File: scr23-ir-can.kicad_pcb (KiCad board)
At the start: 2 copper layers, 27.4 x 27.4 mm, 22 parts, among them J1 22-24AWG, J2 22-24AWG, J3 22-24AWG, J4 22-24AWG, J6 Conn_ST_STDC14, U1 Sparkfun MLX90640 Breakout, U2 AP63205WU, U4 ADM3051CRZ, U5 STM32L431KBUx, U6 AP2127K-3.3

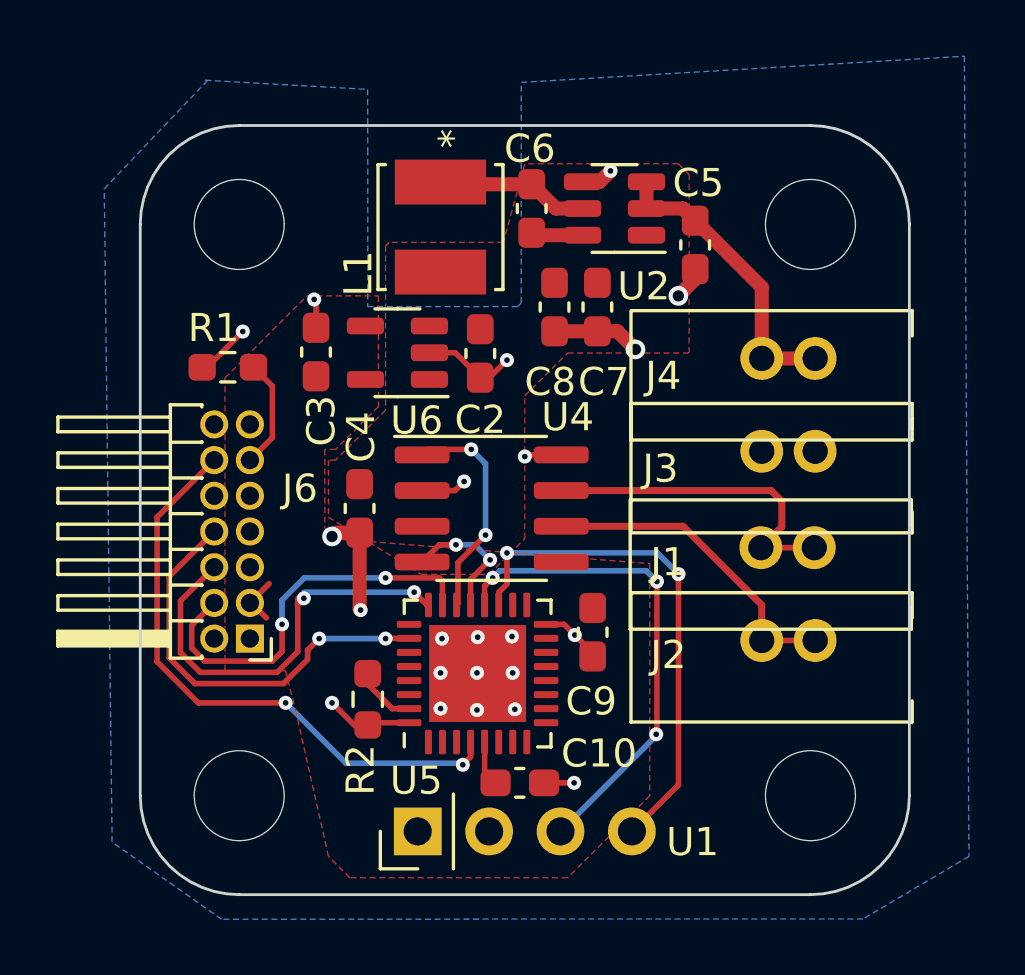
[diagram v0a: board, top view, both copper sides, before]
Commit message: add labels to the solderright bois
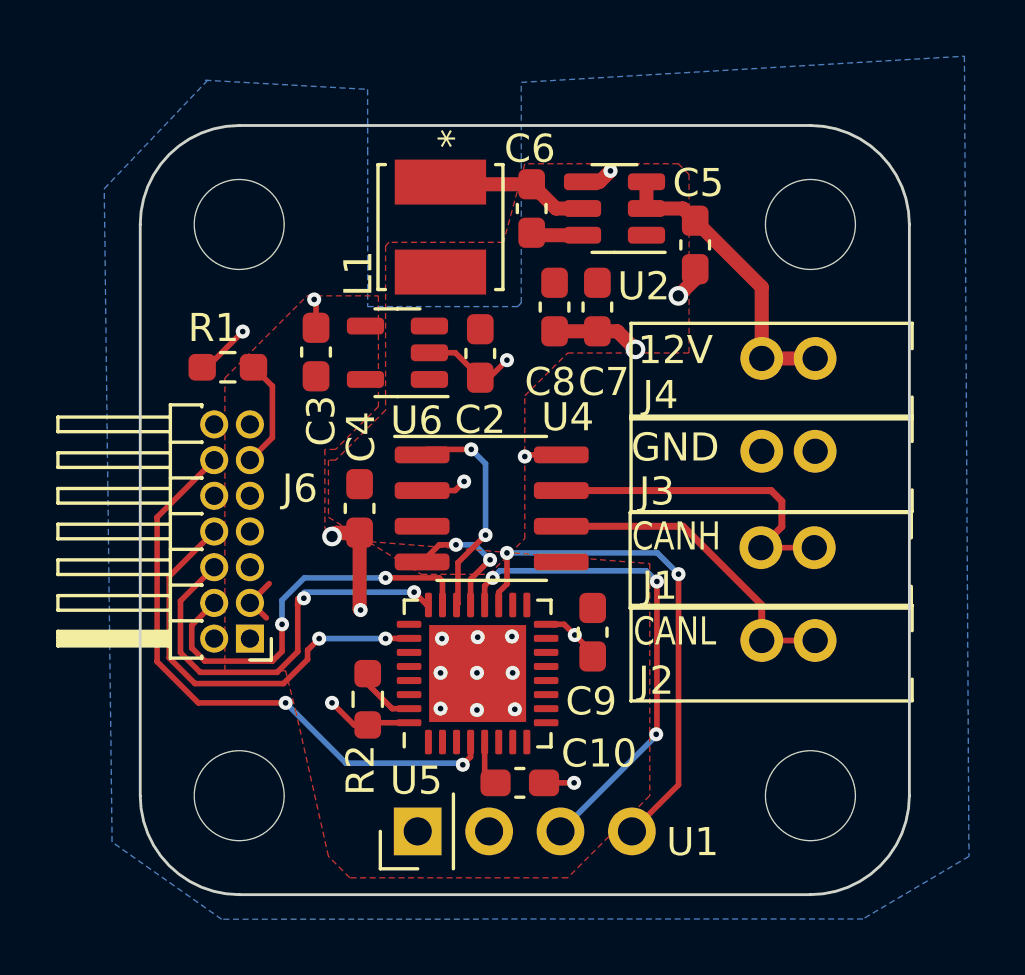
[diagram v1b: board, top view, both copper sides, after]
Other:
- board text added: "12V"
- board text added: "CANH"
- board text added: "CANL"
- board text added: "GND"
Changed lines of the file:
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@@
     (property "ki_description" "CONN TERM WTB 22-24AWG TIN")
     (attr through_hole)
-    (fp_text reference "J1" (at -3.2918 0.5167 unlocked) (layer "F.SilkS")
+    (fp_text reference "J1" (at -3.5966 1.3549 unlocked) (layer "F.SilkS")
         (effects (font (size 1 1) (thickness 0.15)))
     )
@@
         (effects (font (size 1 1) (thickness 0.15)))
     )
-    (fp_line (start -4.65 -1.7) (end 5.35 -1.7)
-      (stroke (width 0.12) (type default)) (layer "F.SilkS"))
-    (fp_line (start -4.65 2.9) (end -4.65 -1.65)
-      (stroke (width 0.12) (type default)) (layer "F.SilkS"))
-    (fp_line (start 5.35 -1.7) (end 5.35 -0.8)
-      (stroke (width 0.12) (type default)) (layer "F.SilkS"))
-    (fp_line (start 5.35 2.15) (end 5.35 2.9)
-      (stroke (width 0.12) (type default)) (layer "F.SilkS"))
-    (fp_line (start 5.35 2.9) (end -4.65 2.9)
+    (fp_line (start -4.65 -1.25) (end 5.35 -1.25)
+      (stroke (width 0.12) (type default)) (layer "F.SilkS"))
+    (fp_line (start -4.65 2.15) (end -4.65 -1.25)
+      (stroke (width 0.12) (type default)) (layer "F.SilkS"))
+    (fp_line (start 5.35 -1.25) (end 5.35 -0.35)
+      (stroke (width 0.12) (type default)) (layer "F.SilkS"))
+    (fp_line (start 5.35 1.375) (end 5.35 2.125)
+      (stroke (width 0.12) (type default)) (layer "F.SilkS"))
+    (fp_line (start 5.35 2.15) (end -4.65 2.15)
       (stroke (width 0.12) (type default)) (layer "F.SilkS"))
     (pad "1" thru_hole circle (at 0 0) (size 1.524 1.524) (drill 0.9) (layers "*.Cu" "*.Mask")
@@
     (property "ki_description" "CONN TERM WTB 22-24AWG TIN")
     (attr through_hole)
-    (fp_text reference "J4" (at -3.5006 0.6183 unlocked) (layer "F.SilkS")
+    (fp_text reference "J4" (at -3.6022 1.3041 unlocked) (layer "F.SilkS")
         (effects (font (size 1 1) (thickness 0.15)))
     )
@@
         (effects (font (size 1 1) (thickness 0.15)))
     )
-    (fp_line (start -4.65 -1.7) (end 5.35 -1.7)
-      (stroke (width 0.12) (type default)) (layer "F.SilkS"))
-    (fp_line (start -4.65 2.9) (end -4.65 -1.65)
-      (stroke (width 0.12) (type default)) (layer "F.SilkS"))
-    (fp_line (start 5.35 -1.7) (end 5.35 -0.8)
-      (stroke (width 0.12) (type default)) (layer "F.SilkS"))
-    (fp_line (start 5.35 2.15) (end 5.35 2.9)
-      (stroke (width 0.12) (type default)) (layer "F.SilkS"))
-    (fp_line (start 5.35 2.9) (end -4.65 2.9)
+    (fp_line (start -4.65 -1.25) (end 5.35 -1.25)
+      (stroke (width 0.12) (type default)) (layer "F.SilkS"))
+    (fp_line (start -4.65 2.15) (end -4.65 -1.25)
+      (stroke (width 0.12) (type default)) (layer "F.SilkS"))
+    (fp_line (start 5.35 -1.25) (end 5.35 -0.35)
+      (stroke (width 0.12) (type default)) (layer "F.SilkS"))
+    (fp_line (start 5.35 1.375) (end 5.35 2.125)
+      (stroke (width 0.12) (type default)) (layer "F.SilkS"))
+    (fp_line (start 5.35 2.15) (end -4.65 2.15)
       (stroke (width 0.12) (type default)) (layer "F.SilkS"))
     (pad "1" thru_hole circle (at 0 0) (size 1.524 1.524) (drill 0.9) (layers "*.Cu" "*.Mask")
@@
     (property "ki_description" "CONN TERM WTB 22-24AWG TIN")
     (attr through_hole)
-    (fp_text reference "J2" (at -3.3228 0.5167 unlocked) (layer "F.SilkS")
+    (fp_text reference "J2" (at -3.7546 1.4311 unlocked) (layer "F.SilkS")
         (effects (font (size 1 1) (thickness 0.15)))
     )
@@
         (effects (font (size 1 1) (thickness 0.15)))
     )
-    (fp_line (start -4.65 -1.7) (end 5.35 -1.7)
-      (stroke (width 0.12) (type default)) (layer "F.SilkS"))
-    (fp_line (start -4.65 2.9) (end -4.65 -1.65)
-      (stroke (width 0.12) (type default)) (layer "F.SilkS"))
-    (fp_line (start 5.35 -1.7) (end 5.35 -0.8)
-      (stroke (width 0.12) (type default)) (layer "F.SilkS"))
-    (fp_line (start 5.35 2.15) (end 5.35 2.9)
-      (stroke (width 0.12) (type default)) (layer "F.SilkS"))
-    (fp_line (start 5.35 2.9) (end -4.65 2.9)
+    (fp_line (start -4.65 -1.25) (end 5.35 -1.25)
+      (stroke (width 0.12) (type default)) (layer "F.SilkS"))
+    (fp_line (start -4.65 2.15) (end -4.65 -1.25)
+      (stroke (width 0.12) (type default)) (layer "F.SilkS"))
+    (fp_line (start 5.35 -1.25) (end 5.35 -0.35)
+      (stroke (width 0.12) (type default)) (layer "F.SilkS"))
+    (fp_line (start 5.35 1.375) (end 5.35 2.125)
+      (stroke (width 0.12) (type default)) (layer "F.SilkS"))
+    (fp_line (start 5.35 2.15) (end -4.65 2.15)
       (stroke (width 0.12) (type default)) (layer "F.SilkS"))
     (pad "1" thru_hole circle (at 0 0) (size 1.524 1.524) (drill 0.9) (layers "*.Cu" "*.Mask")
@@
     (property "ki_description" "CONN TERM WTB 22-24AWG TIN")
     (attr through_hole)
-    (fp_text reference "J3" (at -3.6022 0.6183 unlocked) (layer "F.SilkS")
+    (fp_text reference "J3" (at -3.7292 1.4311 unlocked) (layer "F.SilkS")
         (effects (font (size 1 1) (thickness 0.15)))
     )
@@
         (effects (font (size 1 1) (thickness 0.15)))
     )
-    (fp_line (start -4.65 -1.7) (end 5.35 -1.7)
-      (stroke (width 0.12) (type default)) (layer "F.SilkS"))
-    (fp_line (start -4.65 2.9) (end -4.65 -1.65)
-      (stroke (width 0.12) (type default)) (layer "F.SilkS"))
-    (fp_line (start 5.35 -1.7) (end 5.35 -0.8)
-      (stroke (width 0.12) (type default)) (layer "F.SilkS"))
-    (fp_line (start 5.35 2.15) (end 5.35 2.9)
-      (stroke (width 0.12) (type default)) (layer "F.SilkS"))
-    (fp_line (start 5.35 2.9) (end -4.65 2.9)
+    (fp_line (start -4.65 -1.25) (end 5.35 -1.25)
+      (stroke (width 0.12) (type default)) (layer "F.SilkS"))
+    (fp_line (start -4.65 2.15) (end -4.65 -1.25)
+      (stroke (width 0.12) (type default)) (layer "F.SilkS"))
+    (fp_line (start 5.35 -1.25) (end 5.35 -0.35)
+      (stroke (width 0.12) (type default)) (layer "F.SilkS"))
+    (fp_line (start 5.35 1.375) (end 5.35 2.125)
+      (stroke (width 0.12) (type default)) (layer "F.SilkS"))
+    (fp_line (start 5.35 2.15) (end -4.65 2.15)
       (stroke (width 0.12) (type default)) (layer "F.SilkS"))
     (pad "1" thru_hole circle (at 0 0) (size 1.524 1.524) (drill 0.9) (layers "*.Cu" "*.Mask")
@@
   (gr_arc (start 105.099831 96.452499) (mid 106.130865 93.963364) (end 108.62 92.93233)
     (stroke (width 0.1) (type default)) (layer "Edge.Cuts"))
+  (gr_text "12V" (at 122.7932 101.5071) (layer "F.SilkS")
+    (effects (font (size 1 1) (thickness 0.15)) (justify left bottom))
+  )
+  (gr_text "GND\n" (at 122.5582 104.971) (layer "F.SilkS")
+    (effects (font (size 1 1) (thickness 0.15)) (justify left bottom))
+  )
+  (gr_text "CANH" (at 122.59 108.1365) (layer "F.SilkS")
+    (effects (font (size 1 0.8) (thickness 0.15)) (justify left bottom))
+  )
+  (gr_text "CANL" (at 122.6408 111.5147) (layer "F.SilkS")
+    (effects (font (size 1 0.8) (thickness 0.15)) (justify left bottom))
+  )
   (segment (start 107.303 101.5325) (end 107.477 101.5325) (width 0.2) (layer "F.Cu") (net 2))
   (segment (start 111.3536 99.1861) (end 111.287 99.1195) (width 0.2) (layer "F.Cu") (net 2))
